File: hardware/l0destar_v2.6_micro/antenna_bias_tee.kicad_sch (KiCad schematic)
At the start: 11 parts

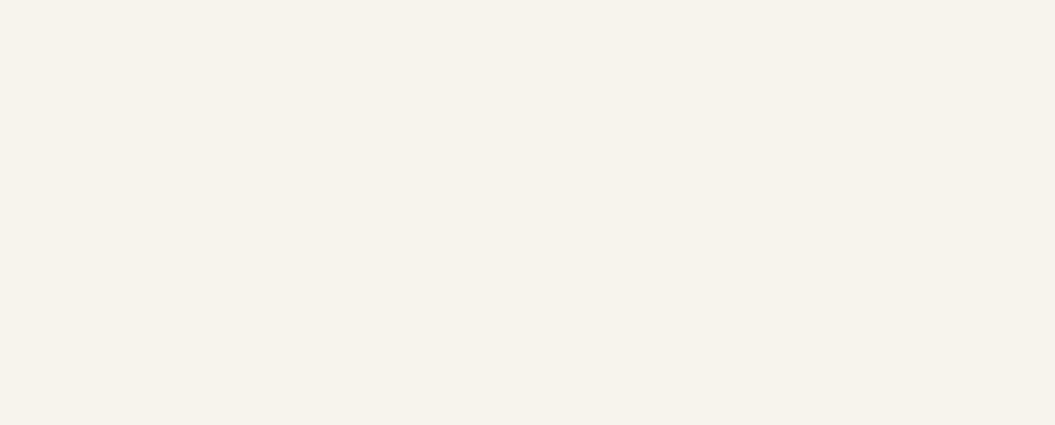
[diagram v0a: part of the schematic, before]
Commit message: update sheet annotations
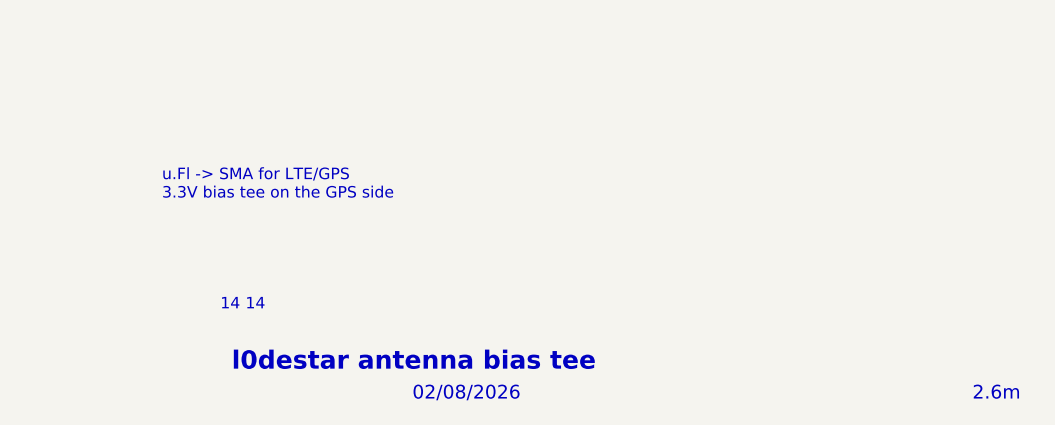
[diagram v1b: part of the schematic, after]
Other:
- note added: "02/08/2026"
- note added: "14"
- note added: "2.6m"
- note added: "l0destar antenna bias tee"
- note added: "u.Fl -> SMA for LTE/GPS 3.3V bias tee on the GPS side"
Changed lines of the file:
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@@
 	(generator_version "10.0")
 	(paper "A4")
+	(text "l0destar antenna bias tee"
+		(exclude_from_sim no)
+		(at 186.817 189.865 0)
+		(effects
+			(font
+				(face "KiCad Font")
+				(size 2.032 2.032)
+				(thickness 0.4064)
+				(bold yes)
+			)
+			(justify left)
+		)
+	)
+	(text "02/08/2026"
+		(exclude_from_sim no)
+		(at 206.883 193.421 0)
+		(effects
+			(font
+				(face "KiCad Font")
+				(size 1.524 1.524)
+				(thickness 0.1905)
+			)
+			(justify left)
+		)
+	)
+	(text "u.Fl -> SMA for LTE/GPS\n3.3V bias tee on the GPS side"
+		(exclude_from_sim no)
+		(at 179.07 170.18 0)
+		(effects
+			(font
+				(size 1.27 1.27)
+			)
+			(justify left)
+		)
+	)
+	(text "14"
+		(exclude_from_sim no)
+		(at 185.547 183.515 0)
+		(effects
+			(font
+				(size 1.27 1.27)
+			)
+			(justify left)
+		)
+	)
+	(text "2.6m"
+		(exclude_from_sim no)
+		(at 269.113 193.421 0)
+		(effects
+			(font
+				(face "KiCad Font")
+				(size 1.524 1.524)
+				(thickness 0.1905)
+			)
+			(justify left)
+		)
+	)
+	(text "14"
+		(exclude_from_sim no)
+		(at 188.341 183.515 0)
+		(effects
+			(font
+				(size 1.27 1.27)
+			)
+			(justify left)
+		)
+	)
 	(junction
 		(at 149.86 50.8)
